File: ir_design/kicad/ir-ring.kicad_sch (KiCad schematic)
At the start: 24 parts, among them J1 JST ZH B5B-ZR, Q1 AO3400A, U1 SY7200A, U2 TEMT6200FX01

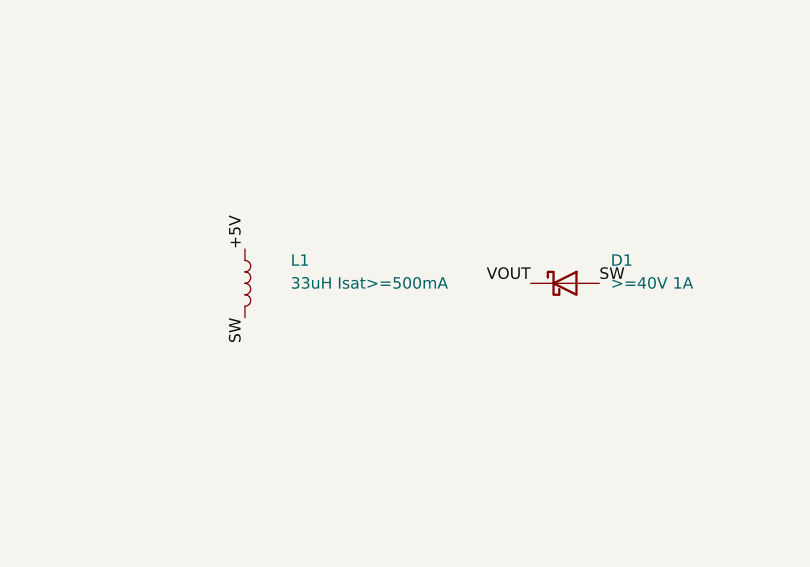
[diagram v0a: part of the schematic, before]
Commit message: feat(ir): validate the light-sensor footprint and pick L1
U2 (TEMT6200FX01, C143695) moves from a generic R_0805 to a footprint drawn
from Vishay's recommended pad: 1.0 x 1.45 mm pads with a 0.6 mm gap, against
R_0805's ~0.8 mm. The generic footprint also had no polarity mark on a part
rated for only 1.5 V VECO. Pad 1 is the collector, matching Q_Photo_NPN, and
is marked "C" on the silkscreen.

L1 is Sunlord SWPA4030S330MT (C83470): 33 uH, 4x4x3 mm, shielded, Isat
1.10 A, Irms 0.84 A, DCR 0.33 typ / 0.43 max ohm. That is about 3x margin on
both current ratings at ~0.36 A peak, and worst-case winding loss is ~31 mW.
Silergy's DCR < 50 mohm guidance is aimed at 2 A designs. KiCad ships no SWPA
footprint, so this one is drawn from Sunlord Table 4-1: 1.10 x 3.70 mm pads,
1.90 mm inner gap.

Both footprints match their datasheets to 0.01 mm. The schematic was
regenerated, the netlist diff is still identical, and ERC reports 0.

Co-Authored-By: Claude Opus 5.5 <noreply@anthropic.com>
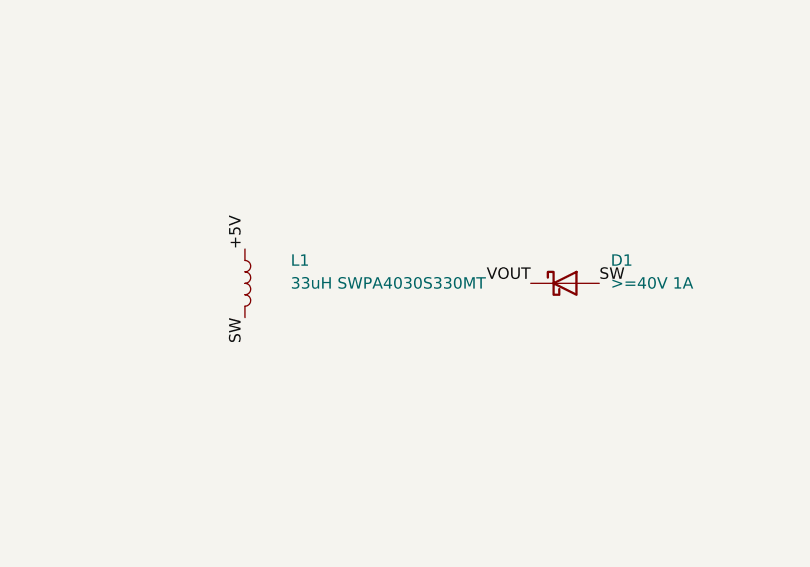
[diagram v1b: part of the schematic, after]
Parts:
- L1: value 33uH Isat>=500mA -> 33uH SWPA4030S330MT; footprint Inductor_SMD:L_Changjiang_FTC404030S -> ir-ring:L_Sunlord_SWPA4030S; LCSC (none) -> C83470
- U2: footprint Resistor_SMD:R_0805_2012Metric -> ir-ring:TEMT6200_0805; LCSC (none) -> C143695

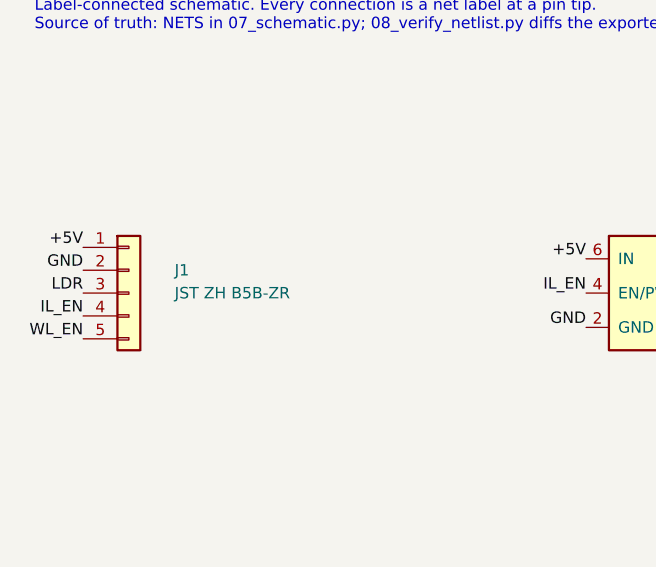
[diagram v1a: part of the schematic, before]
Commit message: feat(ir): place every footprint; J1 is 1.25 mm with a reversed pin map
09_place.py builds the whole board from scratch: outline from geometry.json,
then every footprint with its net, then assertions on the placement geometry.
pcbnew.LoadBoard() corrupts the SWIG type table in this 9.0.8 build (after
it, FootprintLoad and GetDesignSettings return bare SwigPyObjects and the
process segfaults), so the script uses CreateEmptyBoard() and never loads.

J1 correction. The earlier JST ZH 1.5 mm pick was wrong. The connector's
contacts on the back scan measure 1.246 mm pitch, and 4.98 mm between the
outer centres, so the "6 mm" was edge to edge. It is a PicoBlade-class
1.25 mm right-angle THT part with its body on the back. A footprint flipped
to the back and facing outward can only land pad 5 on the stock "+" contact,
so J1 is wired pad 5 = 5V ... pad 1 = WL_EN. The cable order is unchanged.
The script checks all five pads against the measured contacts (all within
0.03 mm) and checks that the body faces outward. Net names go on the back
silkscreen so a 1:1 overlay against the stock board confirms the mapping.

The emitters go on their measured centres, oriented so each cathode faces
the next anode. U2 goes on the stock LDR footprint at r 15.0 / 280.2 deg,
which is under the 9th dome. The converter goes on the back in the top gap:
L1 beside LX, D1 under U1, C2 on D1's cathode. The script checks SW
2.3-2.6 mm, VOUT 1.6 mm and the hot-loop return 5.1 mm. The return closes
through the F.Cu ground plane above, and an explicit check keeps the front
copper there clear; R6/R7 were moved off it to allow that.

Also: U1 moves to the standard SOT-23-6 footprint, since JLCPCB assembles
the board and hand-solder pads only cost room. Emitter thermal vias go to
0.6/0.3 mm for JLCPCB's annular-ring minimum. Schematic UUIDs are now
deterministic so footprints stay linked to their symbols across
regenerations. Reference designators move to the fab layer.

DRC: no errors. Remaining warnings a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
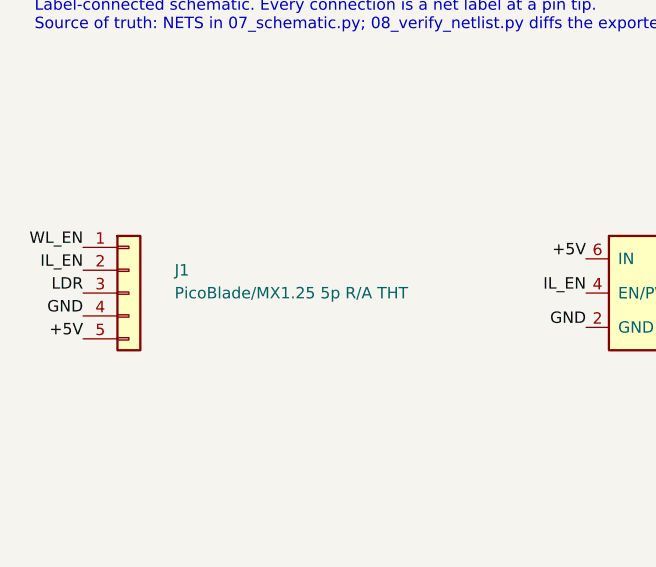
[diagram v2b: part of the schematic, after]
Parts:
- J1: value JST ZH B5B-ZR -> PicoBlade/MX1.25 5p R/A THT; footprint Connector_JST:JST_ZH_B5B-ZR_1x05_P1.50mm_Vertical -> Connector_Molex:Molex_PicoBlade_53048-0510_1x05_P1.25mm_Horizontal
- U1: footprint Package_TO_SOT_SMD:SOT-23-6_Handsoldering -> Package_TO_SOT_SMD:SOT-23-6
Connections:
- net +5V: now also J1.5 (Pin_5); no longer J1.1 (Pin_1)
- net GND: now also J1.4 (Pin_4); no longer J1.2 (Pin_2)
- net IL_EN: now also J1.2 (Pin_2); no longer J1.4 (Pin_4)
- net WL_EN: now also J1.1 (Pin_1); no longer J1.5 (Pin_5)

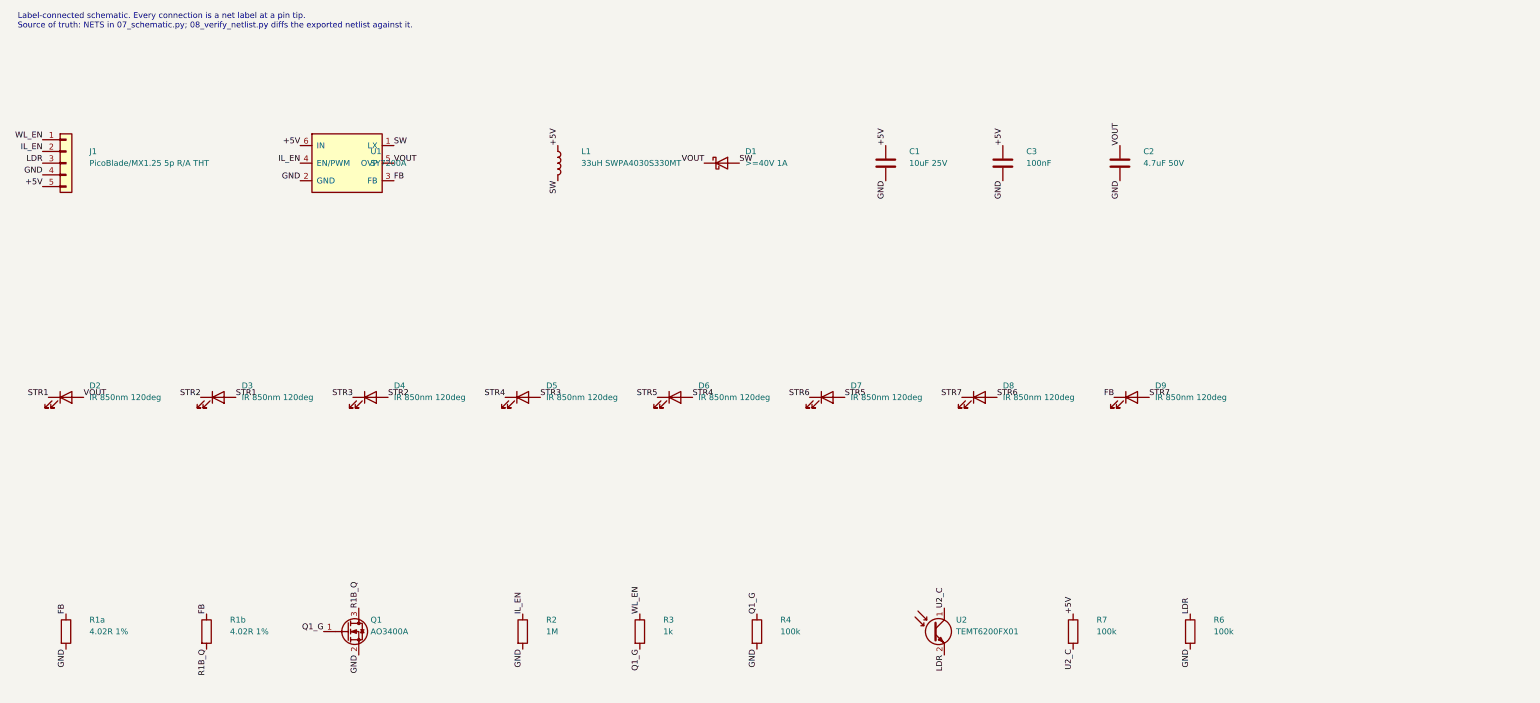
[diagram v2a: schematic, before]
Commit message: fix(ir): draw the schematic with wires and power symbols
The label-only sheet stacked every net name on its pin and was unreadable.
07 now lays out each block and draws real wires, junctions and +5V/GND
power symbols; 08 still diffs the result against NETS (identical), ERC clean.

Power symbols name nets globally (GND, not /GND), so 09 takes net names
from net_names.json and the committed SES/DSN are renamed to match;
DRC with --schematic-parity stays at 0 errors.

Co-Authored-By: Claude Opus 5.5 <noreply@anthropic.com>
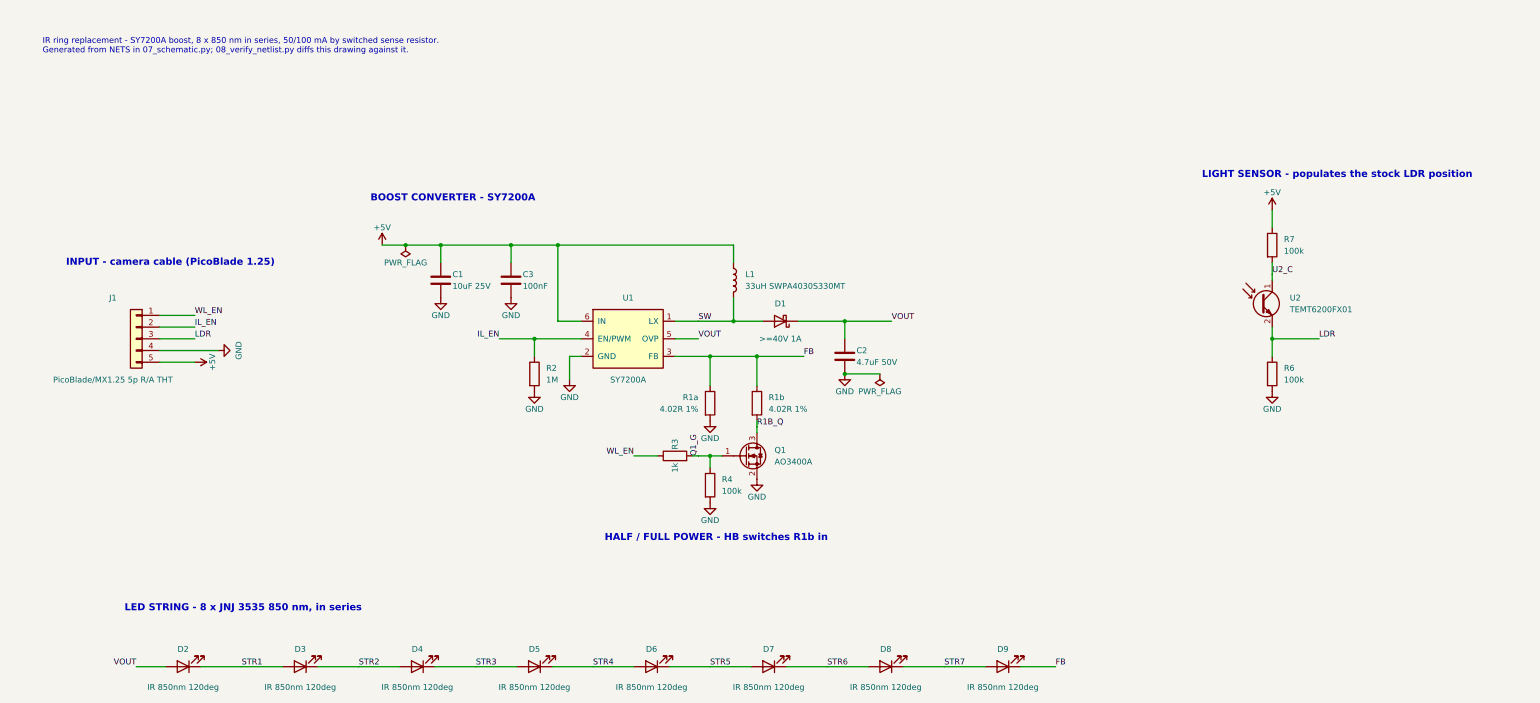
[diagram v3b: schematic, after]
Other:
- note added: "BOOST CONVERTER - SY7200A"
- note added: "HALF / FULL POWER - HB switches R1b in"
- note added: "INPUT - camera cable (PicoBlade 1.25)"
- note added: "IR ring replacement - SY7200A boost, 8 x 850 nm in series, 50/100 mA by switched sense resistor. Generated from NETS in 07_schematic.py; 08_verify_netlist.py diffs this drawing against it."
- note added: "LED STRING - 8 x JNJ 3535 850 nm, in series"
- note added: "LIGHT SENSOR - populates the stock LDR position"
- note removed: "Label-connected schematic. Every connection is a net label at a pin tip. Source of truth: NETS in 07_schematic.py; 08_verify_netlist.py diffs the exported netlist against it."
- moved on the sheet: C1, C2, C3, D1, D2, D3, D4, D5, D6, D7, D8, D9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

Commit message: feat(ir): spread the back side, 0805 passives, test pads
Only the switching loop stays packed in the top gap, now with >= 0.3 mm
courtyard gaps (was 0.03-0.1 mm, with L1/C1/C2 cutting into the thermal
islands). The DC-only half-power switch (Q1, R3, R4) moves to the D7-D8 gap;
09 asserts island, screw-head and courtyard clearances.

- all 0402 passives -> 0805; C2 -> 1206 X7R (C29823) for DC-bias margin
- TP1 VOUT (on D2's VOUT island), TP2 FB, TP3 GND, out of the BOM
- power stage pre-routed and closed on B.Cu; Freerouting re-solved it
  differently every run and stopped finding the VOUT crossing
- LCSC field hidden: it was printed on the silkscreen (78 -> 9 silk warnings)

DRC with --schematic-parity: 0 violations, 0 unconnected, 0 footprint errors.

Co-Authored-By: Claude Opus 5.5 <noreply@anthropic.com>
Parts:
- added TP1: VOUT, TestPoint:TestPoint_Pad_D1.5mm, symbol Connector:TestPoint
- added TP2: FB, TestPoint:TestPoint_Pad_D1.5mm, symbol Connector:TestPoint
- added TP3: GND, TestPoint:TestPoint_Pad_D1.5mm, symbol Connector:TestPoint
- C2: value 4.7uF 50V -> 4.7uF 50V X7R; footprint Capacitor_SMD:C_0805_2012Metric -> Capacitor_SMD:C_1206_3216Metric; LCSC C98192 -> C29823
- C3: footprint Capacitor_SMD:C_0402_1005Metric -> Capacitor_SMD:C_0805_2012Metric; LCSC C307331 -> C49678
- R2: footprint Resistor_SMD:R_0402_1005Metric -> Resistor_SMD:R_0805_2012Metric; LCSC (none) -> C17514
- R3: footprint Resistor_SMD:R_0402_1005Metric -> Resistor_SMD:R_0805_2012Metric; LCSC C11702 -> C17513
- R4, R6, R7: footprint Resistor_SMD:R_0402_1005Metric -> Resistor_SMD:R_0805_2012Metric; LCSC C25741 -> C149504
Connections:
- net FB: now also TP2.1
- net GND: now also TP3.1
- net VOUT: now also TP1.1
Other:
- note added: "TEST PADS - bring-up, back side"

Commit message: feat(ir): JLCPCB two-layer FR4 fab package
11_fab.py builds ir_design/fab/ from the routed board, and refuses to run
unless DRC with schematic parity is clean: gerbers + drill zip, a grouped
JLCPCB BOM, the CPL (both sides, 12 parts on the back), and cross-checks
(drill hits = vias + plated pads, every BOM line has a placement).

The 2 oz order the plan asks for was not legal as drawn:
- board rules raised to JLCPCB's 2 oz floor, 0.16/0.16 mm, re-routed
- PTH ring >= 0.254 mm enforced in ir-ring.kicad_dru; the stock PicoBlade
  footprint left 0.15 mm (under even the 1 oz floor), so J1 gets 1.05 mm
  pads for a 0.275 mm ring
- the VOUT via moved 0.1 mm off U1's LX pad (was 0.150 mm)

J1 is hand-soldered (no LCSC listing found). ORDER.md lists the options
and the placement-preview checks for the custom footprints.

Co-Authored-By: Claude Opus 5.5 <noreply@anthropic.com>
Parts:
- J1: footprint Connector_Molex:Molex_PicoBlade_53048-0510_1x05_P1.25mm_Horizontal -> ir-ring:Molex_PicoBlade_53048-0510_1x05_P1.25mm_Horizontal_Ring0.275
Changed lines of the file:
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@@
 (text "LED STRING - 8 x JNJ 3535 850 nm, in series" (exclude_from_sim no) (at 43.18 147.32 0) (effects (font (size 1.524 1.524) (bold yes)) (justify left)))
 (text "TEST PADS - bring-up, back side" (exclude_from_sim no) (at 226.06 99.06 0) (effects (font (size 1.524 1.524) (bold yes)) (justify left)))
-(symbol (lib_id "Connector_Generic:Conn_01x05") (at 45.72 88.9 0) (mirror y) (unit 1) (exclude_from_sim no) (in_bom yes) (on_board yes) (dnp no)(property "Reference" "J1" (at 40.64 80.01 0) (effects (font (size 1.27 1.27))))(property "Value" "PicoBlade/MX1.25 5p R/A THT" (at 40.64 97.79 0) (effects (font (size 1.27 1.27))))(property "Footprint" "Connector_Molex:Molex_PicoBlade_53048-0510_1x05_P1.25mm_Horizontal" (at 45.72 88.9 0) (effects (font (size 1.27 1.27)) (hide yes)))(property "Datasheet" "~" (at 45.72 88.9 0) (effects (font (size 1.27 1.27)) (hide yes)))(property "Description" "" (at 45.72 88.9 0) (effects (font (size 1.27 1.27)) (hide yes)))(property "LCSC" "" (at 45.72 88.9 0) (effects (font (size 1.27 1.27)) (hide yes)))(pin "1")(pin "2")(pin "3")(pin "4")(pin "5")(instances (project "ir-ring" (path "/cdf836e3-5e27-575e-8189-40b446b7a956" (reference "J1") (unit 1)))))
+(symbol (lib_id "Connector_Generic:Conn_01x05") (at 45.72 88.9 0) (mirror y) (unit 1) (exclude_from_sim no) (in_bom yes) (on_board yes) (dnp no)(property "Reference" "J1" (at 40.64 80.01 0) (effects (font (size 1.27 1.27))))(property "Value" "PicoBlade/MX1.25 5p R/A THT" (at 40.64 97.79 0) (effects (font (size 1.27 1.27))))(property "Footprint" "ir-ring:Molex_PicoBlade_53048-0510_1x05_P1.25mm_Horizontal_Ring0.275" (at 45.72 88.9 0) (effects (font (size 1.27 1.27)) (hide yes)))(property "Datasheet" "~" (at 45.72 88.9 0) (effects (font (size 1.27 1.27)) (hide yes)))(property "Description" "" (at 45.72 88.9 0) (effects (font (size 1.27 1.27)) (hide yes)))(property "LCSC" "" (at 45.72 88.9 0) (effects (font (size 1.27 1.27)) (hide yes)))(pin "1")(pin "2")(pin "3")(pin "4")(pin "5")(instances (project "ir-ring" (path "/cdf836e3-5e27-575e-8189-40b446b7a956" (reference "J1") (unit 1)))))
 (symbol (lib_id "ir-ring:SY7200A") (at 152.4 88.9 0) (unit 1) (exclude_from_sim no) (in_bom yes) (on_board yes) (dnp no)(property "Reference" "U1" (at 152.4 80.01 0) (effects (font (size 1.27 1.27))))(property "Value" "SY7200A" (at 152.4 97.79 0) (effects (font (size 1.27 1.27))))(property "Footprint" "Package_TO_SOT_SMD:SOT-23-6" (at 152.4 88.9 0) (effects (font (size 1.27 1.27)) (hide yes)))(property "Datasheet" "~" (at 152.4 88.9 0) (effects (font (size 1.27 1.27)) (hide yes)))(property "Description" "" (at 152.4 88.9 0) (effects (font (size 1.27 1.27)) (hide yes)))(property "LCSC" "C107309" (at 152.4 88.9 0) (effects (font (size 1.27 1.27)) (hide yes)))(pin "6")(pin "4")(pin "2")(pin "1")(pin "5")(pin "3")(instances (project "ir-ring" (path "/cdf836e3-5e27-575e-8189-40b446b7a956" (reference "U1") (unit 1)))))
 (symbol (lib_id "Device:L") (at 175.26 76.2 0) (unit 1) (exclude_from_sim no) (in_bom yes) (on_board yes) (dnp no)(property "Reference" "L1" (at 177.79999999999998 74.93 0) (effects (font (size 1.27 1.27)) (justify left)))(property "Value" "33uH SWPA4030S330MT" (at 177.79999999999998 77.47 0) (effects (font (size 1.27 1.27)) (justify left)))(property "Footprint" "ir-ring:L_Sunlord_SWPA4030S" (at 175.26 76.2 0) (effects (font (size 1.27 1.27)) (hide yes)))(property "Datasheet" "~" (at 175.26 76.2 0) (effects (font (size 1.27 1.27)) (hide yes)))(property "Description" "" (at 175.26 76.2 0) (effects (font (size 1.27 1.27)) (hide yes)))(property "LCSC" "C83470" (at 175.26 76.2 0) (effects (font (size 1.27 1.27)) (hide yes)))(pin "1")(pin "2")(instances (project "ir-ring" (path "/cdf836e3-5e27-575e-8189-40b446b7a956" (reference "L1") (unit 1)))))
